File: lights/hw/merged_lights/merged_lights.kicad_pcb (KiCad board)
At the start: 2 copper layers, 70 x 100 mm, 62 parts, among them J1 Conn_01x08, J2 Conn_01x08, J3 AVR-ISP-6, J4 Conn_01x02, J5 Conn_01x02, J6 Conn_01x02, J7 Conn_01x08, J8 Conn_01x02, J9 Conn_01x08, Q1 AO3400A, Q2 AO3400A, Q3 AO3400A, Q4 AO3400A, Q5 AO3400A, Q6 AO3400A, Q7 AO3400A, Q8 AO3400A, SW1 SW_Push, U1 ATmega328P-A, U2 ADXL345BCCZ

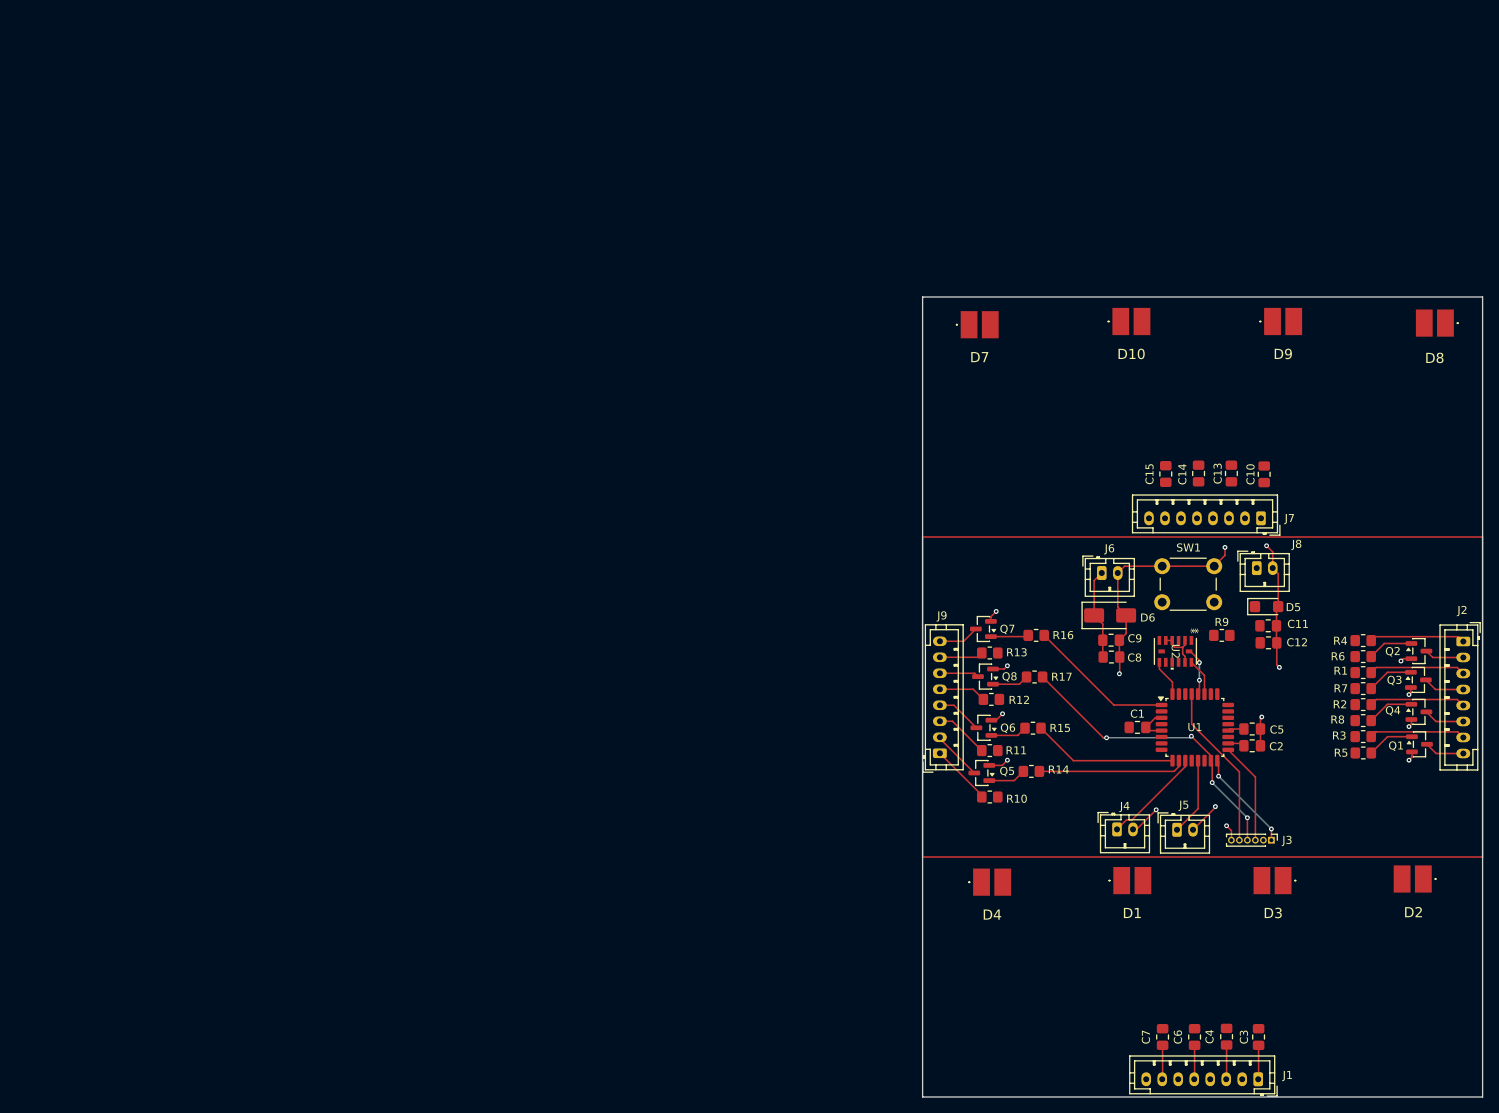
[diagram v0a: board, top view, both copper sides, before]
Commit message: Unpolished final draft. Need mousebites, proper labelling, etc
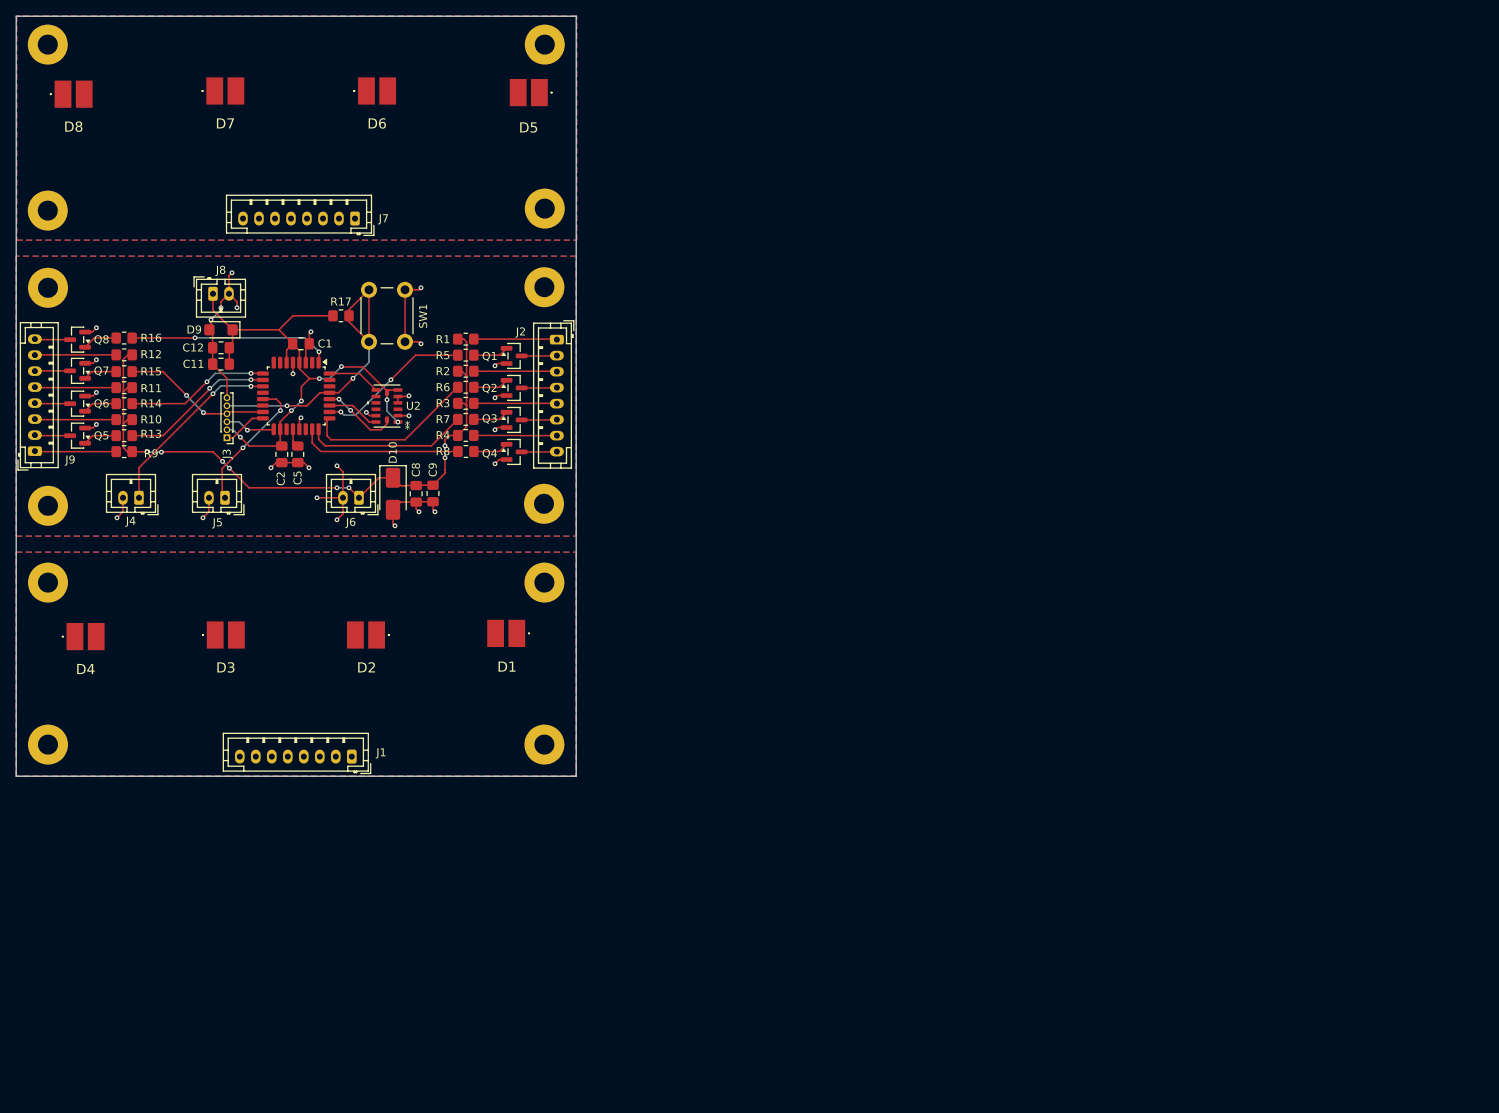
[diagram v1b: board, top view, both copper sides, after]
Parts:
- removed C10, C13, C14, C15, C3, C4, C6, C7: C, Capacitor_SMD:C_0805_2012Metric_Pad1.18x1.45mm_HandSolder
- added H1: MountingHole_Pad, MountingHole:MountingHole_2.5mm_Pad, F.Cu at (78.1, 46.1)
- added H10: MountingHole_Pad, MountingHole:MountingHole_2.5mm_Pad, F.Cu at (16.1, 36.5)
- added H11: MountingHole_Pad, MountingHole:MountingHole_2.5mm_Pad, F.Cu at (78.1, 103.2)
- added H12: MountingHole_Pad, MountingHole:MountingHole_2.5mm_Pad, F.Cu at (78.2, 36.2)
- added H2: MountingHole_Pad, MountingHole:MountingHole_2.5mm_Pad, F.Cu at (16.1, 46.1)
- added H3: MountingHole_Pad, MountingHole:MountingHole_2.5mm_Pad, F.Cu at (16.1, 73.4)
- added H4: MountingHole_Pad, MountingHole:MountingHole_2.5mm_Pad, F.Cu at (78.1, 73.2)
- added H5: MountingHole_Pad, MountingHole:MountingHole_2.5mm_Pad, F.Cu at (16.1, 83.0)
- added H6: MountingHole_Pad, MountingHole:MountingHole_2.5mm_Pad, F.Cu at (16.1, 103.2)
- added H7: MountingHole_Pad, MountingHole:MountingHole_2.5mm_Pad, F.Cu at (78.1, 83.0)
- added H8: MountingHole_Pad, MountingHole:MountingHole_2.5mm_Pad, F.Cu at (16.1, 15.8)
- added H9: MountingHole_Pad, MountingHole:MountingHole_2.5mm_Pad, F.Cu at (78.2, 15.8)
- moved J3 139.9 mm to (38.5, 64.9), turned to 180 degrees
- moved C12 136.0 mm to (37.7, 53.6), turned to 180 degrees
- moved D9 135.2 mm to (37.7, 51.4), turned to 180 degrees
- moved C11 134.9 mm to (37.7, 55.7), turned to 180 degrees
- moved J8 134.9 mm to (36.7, 46.9)
- moved J4 129.1 mm to (27.4, 72.4), turned to 180 degrees
- moved C2 126.7 mm to (45.3, 67.0), turned to -90 degrees
- moved J5 126.0 mm to (38.2, 72.4), turned to 180 degrees
- moved C5 124.1 mm to (47.3, 67.0), turned to -90 degrees
- moved R13 120.9 mm to (25.6, 64.6)
- moved Q5 120.6 mm to (19.8, 64.6)
- moved R14 120.6 mm to (25.6, 60.6)
- moved Q6 120.3 mm to (19.8, 60.6)
- moved J1 120.3 mm to (54.1, 104.8)
- moved R15 120.0 mm to (25.6, 56.6)
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- renumbered D2 to D1, D6 to D10, D3 to D2, D1 to D3, D8 to D5, D9 to D6, D10 to D7, D7 to D8, D5 to D9, Q2 to Q1, Q3 to Q2, Q4 to Q3, Q1 to Q4, Q8 to Q7, Q7 to Q8, R4 to R1, R11 to R10, R12 to R11, R13 to R12, R14 to R13, R15 to R14, R17 to R15, R9 to R17, R1 to R2, R2 to R3, R3 to R4, R6 to R5, R7 to R6, R8 to R7, R5 to R8, R10 to R9
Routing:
- net +12V: track 11.3 -> 82.0 mm, vias 0 -> 8
- net +3.3V: track 2.09 -> 68.9 mm, vias 0 -> 7
- net /HLED2: track 0.00 -> 21.6 mm
- net /HLED4: track 0.00 -> 20.4 mm
- net /HLED3: track 0.00 -> 20.4 mm
- net /HLED1: track 0.00 -> 19.3 mm, vias 0 -> 2
- net /TLED3: track 37.7 -> 18.6 mm, vias 4 -> 2
- net /RESET: track 20.7 -> 37.6 mm, vias 0 -> 2
- net /Button1: track 12.5 -> 23.5 mm, vias 0 -> 2
- net /Button2: track 9.73 -> 17.4 mm, vias 0 -> 2
- net Net-(J3-MISO): track 12.7 -> 5.50 mm, vias 2 -> 0
- net /TLED4: track 18.3 -> 25.5 mm, vias 0 -> 2
- net GND: track 81.4 -> 88.0 mm, vias 16 -> 30
- net Net-(J3-SCK): track 12.7 -> 6.33 mm, vias 0 -> 1
- net /TLED3.1: track 5.96 -> 10.5 mm
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- added copper zone on B.Cu, net GND
- added copper zone on F.Cu, net GND
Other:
- board size 70 x 100 mm -> 70 x 95 mm
